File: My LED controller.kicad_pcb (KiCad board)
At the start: 2 copper layers, 50 x 75 mm, 36 parts, among them J1 AMPHENOL_SPI HDR-20021121-000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, J2 Power SEL, SW3 -, SW4 +, SW5 MODE, SW6 POWER, U1 ESP32-DevKitM-1, U4 SN74AHCT125PWR, U5 AHT20_C2757850, U9 LED_STRIP_CONN

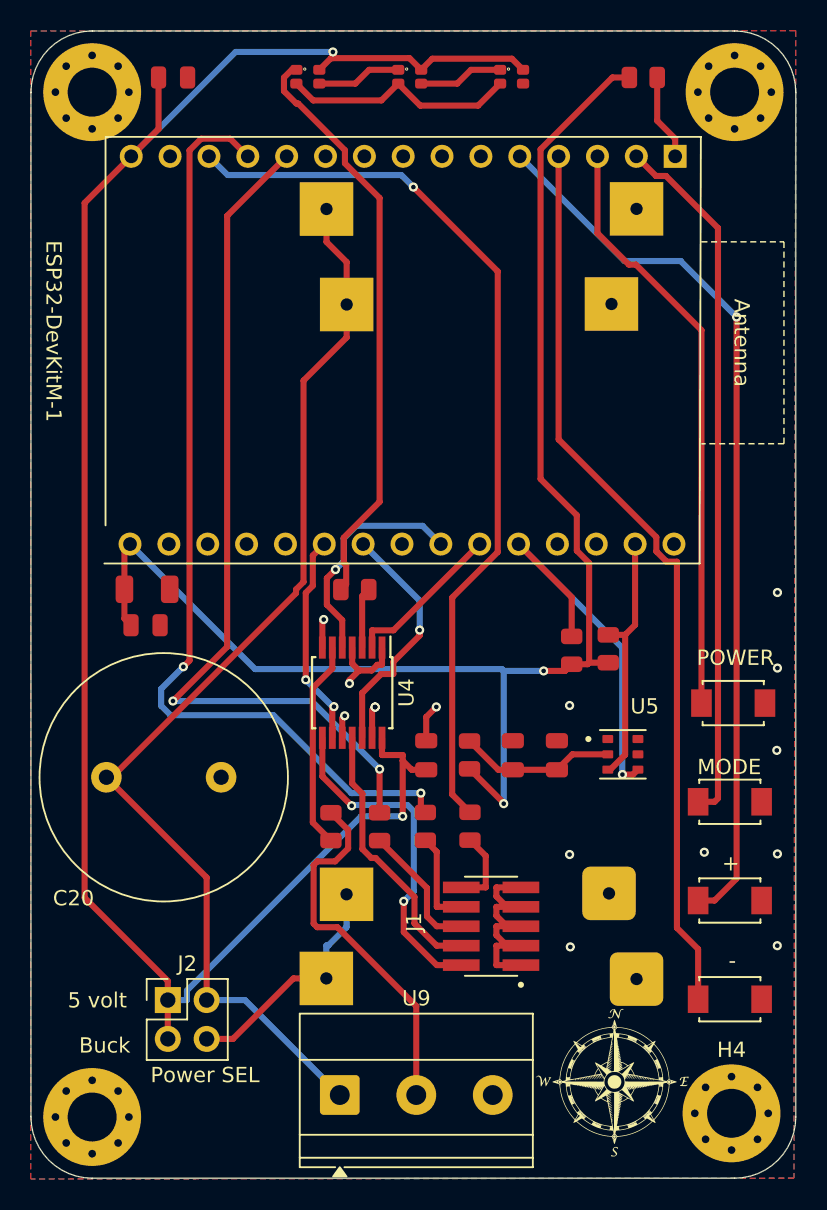
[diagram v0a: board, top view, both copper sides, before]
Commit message: Swap Q1 gate bias resistors: R5 100k (to VIN_RAW), R6 10k (to GND) for better PMOS turn-on at 5V input
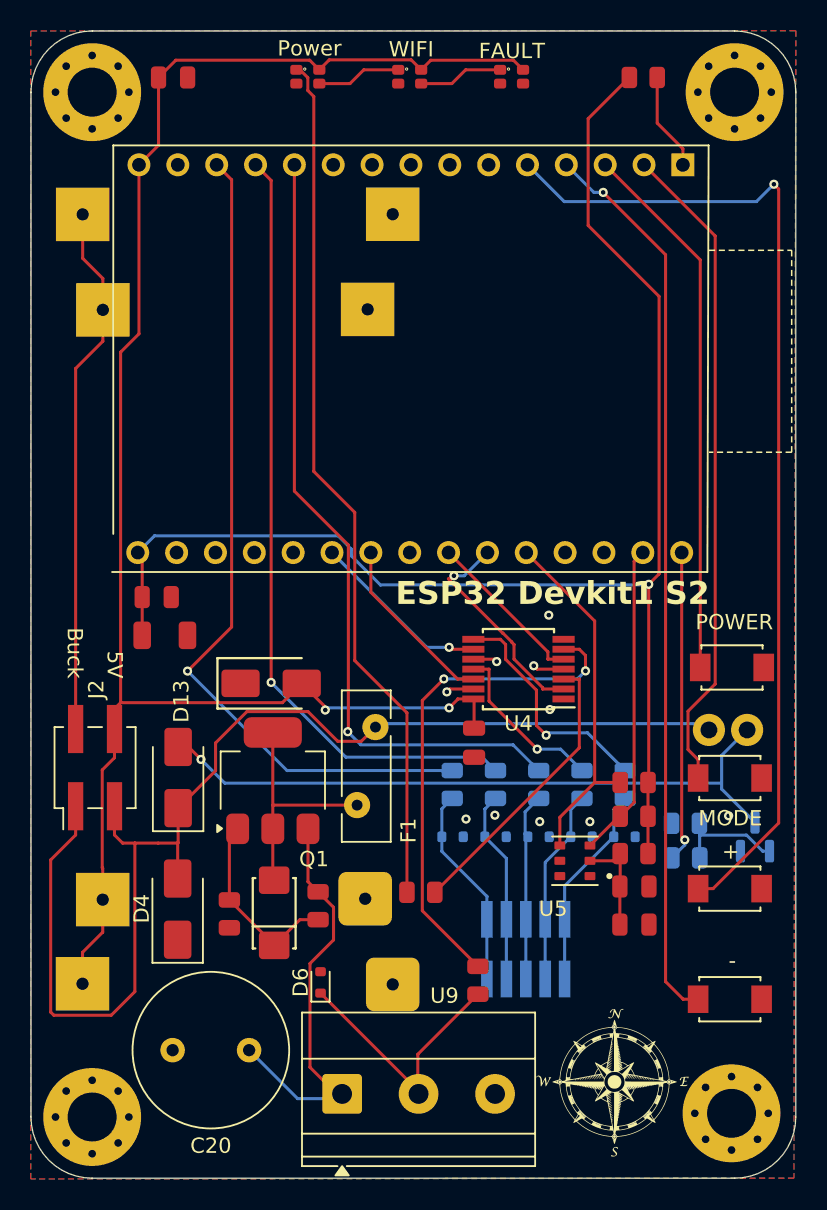
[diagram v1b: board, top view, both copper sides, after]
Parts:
- added D10: ESD5Z5.0T1G, Diode_SMD:D_SOD-523, B.Cu at (158.6, 107.7)
- added D11: ESD5Z5.0T1G, Diode_SMD:D_SOD-523, B.Cu at (161.4, 107.7)
- added D12: 1SMA5927A, PCM_JLCPCB:D_DO-214AC(SMA), F.Cu at (138.5, 112.6)
- added D13: US1M, Diode_SMD:D_SMA, F.Cu at (132.2, 103.8)
- added D4: SMAJ26CA, Diode_SMD:D_SMA, F.Cu at (132.2, 112.4)
- added D5: SMAJ5.0CA, PCM_JLCPCB:D_SMA, F.Cu at (138.3, 97.6)
- added D6: ESD5Z5.0T1G, Diode_SMD:D_SOD-523, F.Cu at (141.6, 117.2)
- added D7: ESD5Z5.0T1G, Diode_SMD:D_SOD-523, B.Cu at (150.2, 107.7)
- added D8: ESD5Z5.0T1G, Diode_SMD:D_SOD-523, B.Cu at (153.0, 107.7)
- added D9: ESD5Z5.0T1G, Diode_SMD:D_SOD-523, B.Cu at (155.8, 107.7)
- added F1: PTC RESET FUSE 700mA TH, Fuse:Fuse_Bourns_MF-RHT100, F.Cu at (143.9, 105.6)
- added J3: Fan Control, digikey-footprints:PinHeader_1x2_P2.5mm_Drill1.1mm, B.Cu at (169.4, 100.7)
- added Q1: BSP322PH6327, Package_TO_SOT_SMD:SOT-223, F.Cu at (138.4, 104.0)
- added Q2: AO3400A, PCM_JLCPCB:Q_SOT-23, B.Cu at (170.0, 107.7)
- added R10: 100kΩ, PCM_JLCPCB:R_0805, B.Cu at (165.4, 106.8)
- added R5: 10kΩ, PCM_JLCPCB:R_0805, F.Cu at (141.4, 112.2)
- added R6: 100kΩ, PCM_JLCPCB:R_0805, F.Cu at (135.6, 112.7)
- added R7: 100Ω, PCM_JLCPCB:R_0805, B.Cu at (161.5, 104.2)
- added R8: 100Ω, PCM_JLCPCB:R_0805, B.Cu at (158.7, 104.2)
- added R9: 100Ω, PCM_JLCPCB:R_0805, B.Cu at (165.4, 109.0)
- C20: footprint Capacitor_THT:C_Radial_D16.0mm_H25.0mm_P7.50mm -> Capacitor_THT:C_Radial_D10.0mm_H12.5mm_P5.00mm
- J1: value AMPHENOL_SPI HDR-20021121-00010C4LF -> AMPHENOL_SPI HDR; moved to B.Cu
- J2: footprint Connector_PinHeader_2.54mm:PinHeader_2x02_P2.54mm_Vertical -> Connector_PinHeader_2.54mm:PinHeader_2x02_P2.54mm_Vertical_SMD
- R2, R3, R4: moved to B.Cu
- moved R16 20.3 mm to (148.1, 111.3)
- moved C20 20.1 mm to (136.9, 121.6), turned to 180 degrees
- moved BUCK1 15.9 mm to (140.0, 75.2)
- moved J2 15.9 mm to (126.8, 103.1), turned to 90 degrees
- moved R15 13.9 mm to (151.8, 117.0), turned to -90 degrees
- moved C18 13.6 mm to (162.1, 113.4), turned to 0 degrees
- moved R14 12.5 mm to (162.1, 108.8), turned to 180 degrees
- moved R12 11.1 mm to (162.1, 106.3), turned to 180 degrees
- moved U4 11.0 mm to (154.5, 96.7), turned to 180 degrees
- moved R2 10.8 mm to (155.8, 104.2)
- moved C17 9.96 mm to (162.1, 110.9), turned to 0 degrees
- moved R13 9.55 mm to (162.1, 104.1), turned to 180 degrees
- moved U5 7.63 mm to (158.2, 109.2), turned to 180 degrees
- moved R3 5.34 mm to (153.0, 104.2)
- moved C19 3.24 mm to (151.6, 101.5), turned to 90 degrees
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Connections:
- BUCK1 pad 2: VIN -> Net-(BUCK1-+Vin)
- BUCK1 pad 4: Net-(BUCK1-+Vout) -> +5V_CTRL
- C1 pad 1: +5v -> +5V_CTRL
- C19 pad 2: +5v -> +5V_CTRL
- C20 pad 1: VIN -> VIN_RAW
- D1 pad 2: +5v -> +5V_CTRL
- D2 pad 2: +5v -> +5V_CTRL
- D3 pad 2: +5v -> +5V_CTRL
- J1 pad 1: Net-(J1-Pad1) -> Net-(D11-K)
- J1 pad 10: Net-(J1-Pad10) -> Net-(D7-K)
- J1 pad 2: 3Y -> Net-(D11-K)
- J1 pad 3: Net-(J1-Pad1) -> Net-(D10-K)
- J1 pad 4: 4Y -> Net-(D10-K)
- J1 pad 5: Net-(J1-Pad1) -> Net-(D9-K)
- J1 pad 6: Net-(J1-Pad6) -> Net-(D9-K)
- J1 pad 7: Net-(J1-Pad1) -> Net-(D8-K)
- J1 pad 8: Net-(J1-Pad8) -> Net-(D8-K)
- J1 pad 9: Net-(J1-Pad1) -> Net-(D7-K)
- J2 pad 1: +5v -> VIN_CLAMPED
- J2 pad 2: VIN -> Net-(BUCK1-+Vin)
- J2 pad 3: +5v -> VIN_CLAMPED
- J2 pad 4: Net-(BUCK1-+Vout) -> +5V_CTRL
- R2 pad 2: Net-(J1-Pad6) -> Net-(D9-K)
- R3 pad 2: Net-(J1-Pad8) -> Net-(D8-K)
- R4 pad 2: Net-(J1-Pad10) -> Net-(D7-K)
- U1 pad 15: +5v -> +5V_CTRL
- U1 pad 30: unconnected-(U1-GPIO23-Pad30) -> GPIO23
- U4 pad 14: +5v -> +5V_CTRL
- U9 pad 1: VIN -> VIN_RAW
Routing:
- net +5v: track 127.0 -> 0.00 mm, vias 2 -> 0
- net +5V_CTRL: track 0.00 -> 113.6 mm, vias 0 -> 2
- net VIN_CLAMPED: track 0.00 -> 80.7 mm
- net VIN: track 73.0 -> 0.00 mm
- net Net-(D13-A): track 0.00 -> 44.2 mm, vias 0 -> 1
- net Net-(BUCK1-+Vin): track 0.00 -> 34.9 mm
- net VIN_RAW: track 0.00 -> 27.2 mm
- net GND: track 28.9 -> 5.44 mm, vias 15 -> 10
- net GPIO23: track 0.00 -> 20.4 mm, vias 0 -> 1
- net LED_STRIP: track 13.6 -> 33.0 mm, vias 0 -> 2
- net Net-(D1-DOUT): track 38.3 -> 56.9 mm
- net Net-(BUCK1-+Vout): track 15.6 -> 0.00 mm
- net VIN_REVPROT: track 0.00 -> 15.2 mm
- net STATUS_LED: track 3.97 -> 18.9 mm
- net Net-(J1-Pad1): track 14.3 -> 0.00 mm
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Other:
- board text added: "5V"
- board text added: "ESP32 Devkit1 S2"
- board text added: "FAN"
- board text added: "Spare Outputs"
- board text removed: "5 volt"

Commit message: Implement pin remap docs and add spare AHCT125 SMT breakout header
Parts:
- added J4: SPARE_OUT_HDR, Connector_PinHeader_2.54mm:PinHeader_2x02_P2.54mm_Vertical_SMD, F.Cu at (126.8, 94.2)
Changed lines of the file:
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@@
 		)
+	)
+	(footprint "Connector_PinHeader_2.54mm:PinHeader_2x02_P2.54mm_Vertical_SMD"
+		(layer "F.Cu")
+		(at 126.82 94.25 90)
+		(descr "surface-mounted straight pin header, 2x02, 2.54mm pitch, double rows")
+		(tags "Surface mounted pin header SMD 2x02 2.54mm double row")
+		(property "Reference" "J4"
+			(at 5.11 0.08 90)
+			(layer "F.SilkS")
+			(effects
+				(font
+					(size 1 1)
+					(thickness 0.15)
+				)
+			)
+		)
+		(property "Value" "SPARE_OUT_HDR"
+			(at 0 3.65 90)
+			(layer "F.Fab")
+			(effects
+				(font
+					(size 1 1)
+					(thickness 0.15)
+				)
+			)
+		)
+		(property "Datasheet" "~"
+			(at 0 0 90)
+			(layer "F.Fab")
+			(hide yes)
+			(effects
+				(font
+					(size 1.27 1.27)
+					(thickness 0.15)
+				)
+			)
+		)
+		(property "Description" "Generic connector, double row, 02x02, odd/even pin numbering scheme (row 1 odd numbers, row 2 even numbers), script generated (kicad-library-utils/schlib/autogen/connector/)"
+			(at 0 0 90)
+			(layer "F.Fab")
+			(hide yes)
+			(effects
+				(font
+					(size 1.27 1.27)
+					(thickness 0.15)
+				)
+			)
+		)
+		(property ki_fp_filters "Connector*:*_2x??_*")
+		(sheetname "/")
+		(sheetfile "My LED controller.kicad_sch")
+		(attr smd)
+		(pad "1" smd rect
+			(at -2.525 -1.27 90)
+			(size 3.15 1)
+			(layers "F.Cu" "F.Mask" "F.Paste")
+			(net 11 "3Y")
+			(pinfunction "Pin_1")
+			(pintype "passive")
+		)
+		(pad "2" smd rect
+			(at 2.525 -1.27 90)
+			(size 3.15 1)
+			(layers "F.Cu" "F.Mask" "F.Paste")
+			(net 10 "4Y")
+			(pinfunction "Pin_2")
+			(pintype "passive")
+		)
+		(pad "3" smd rect
+			(at -2.525 1.27 90)
+			(size 3.15 1)
+			(layers "F.Cu" "F.Mask" "F.Paste")
+			(net 1 "GND")
+			(pinfunction "Pin_3")
+			(pintype "passive")
+		)
+		(pad "4" smd rect
+			(at 2.525 1.27 90)
+			(size 3.15 1)
+			(layers "F.Cu" "F.Mask" "F.Paste")
+			(net 3 "+5V_CTRL")
+			(pinfunction "Pin_4")
+			(pintype "passive")
+		)
+		(embedded_fonts no)
 	)
 	(footprint "1My_Parts_ Passive:10mm LOGO"
